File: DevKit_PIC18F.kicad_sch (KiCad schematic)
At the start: 25 parts, among them J1 PIC_ICSP_ICD, J2 USB_B, J4 RA_PORT, J5 RB_PORT, J6 RD_PORT, J7 RC_PORT, J8 RE_PORT, J9 2P_UART, SW1 SW_DIP, X1 16MHz

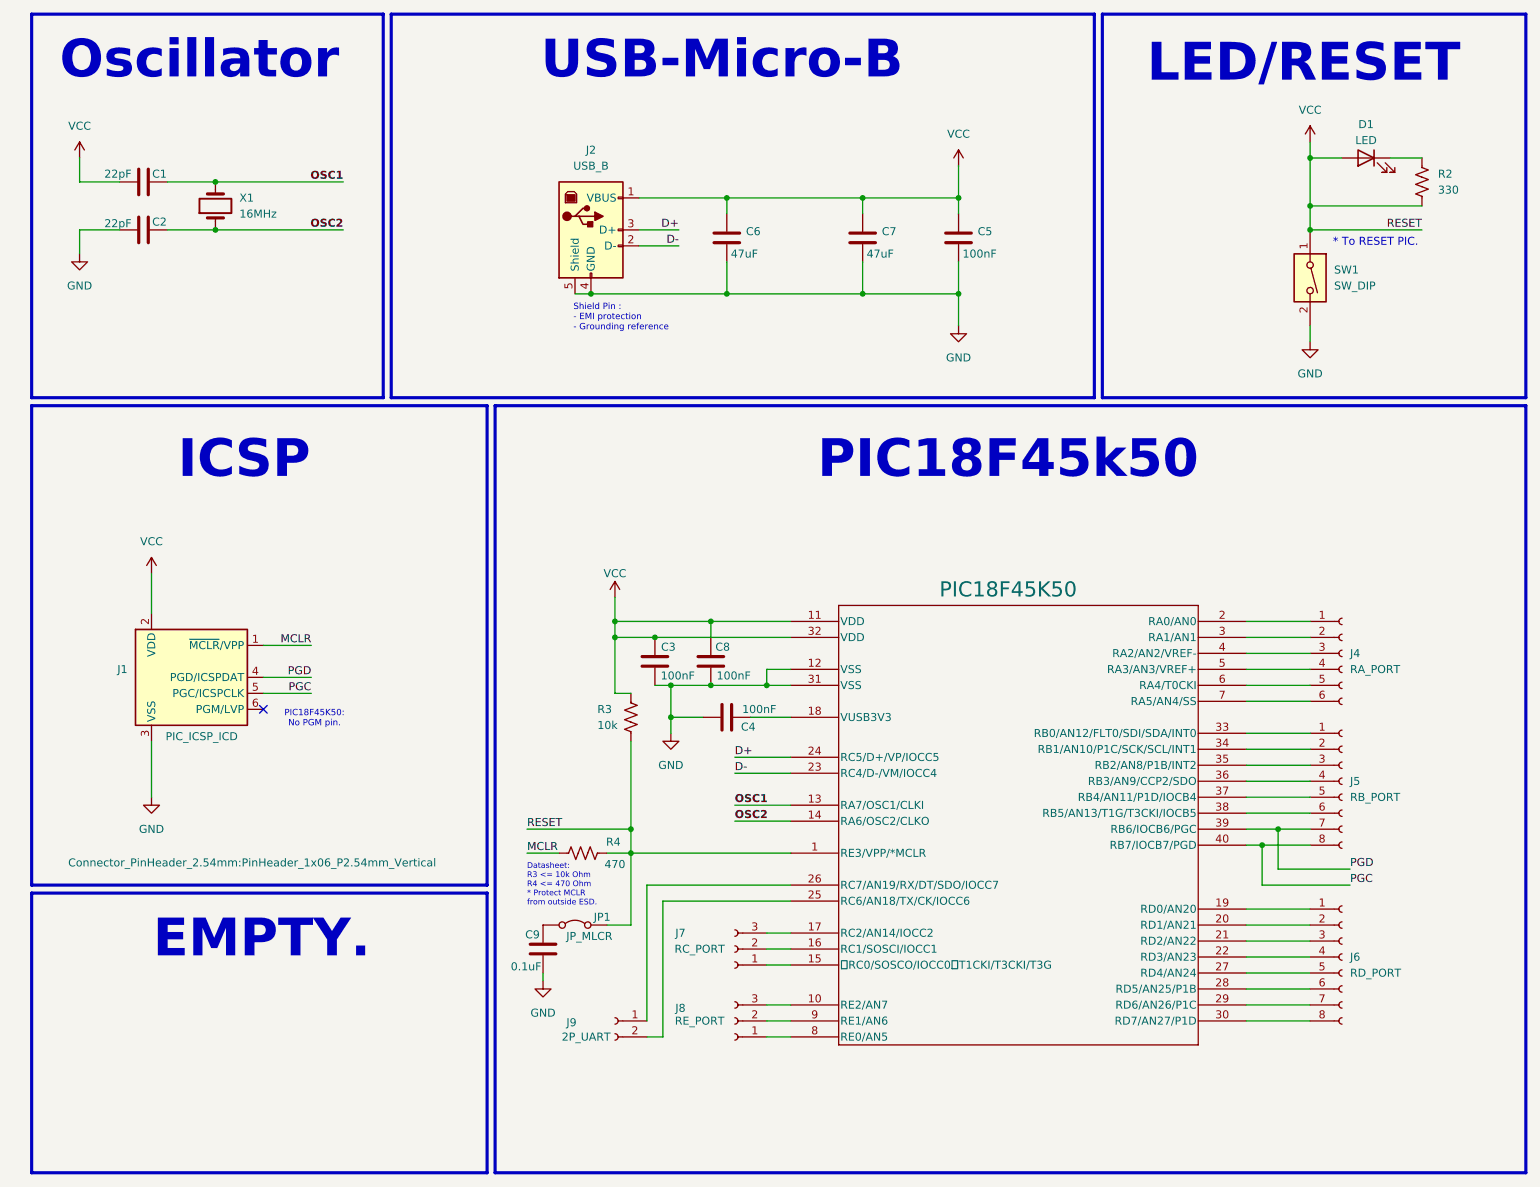
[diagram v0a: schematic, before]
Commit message: Change USB-B -> USB-C & Added EdgeCut.
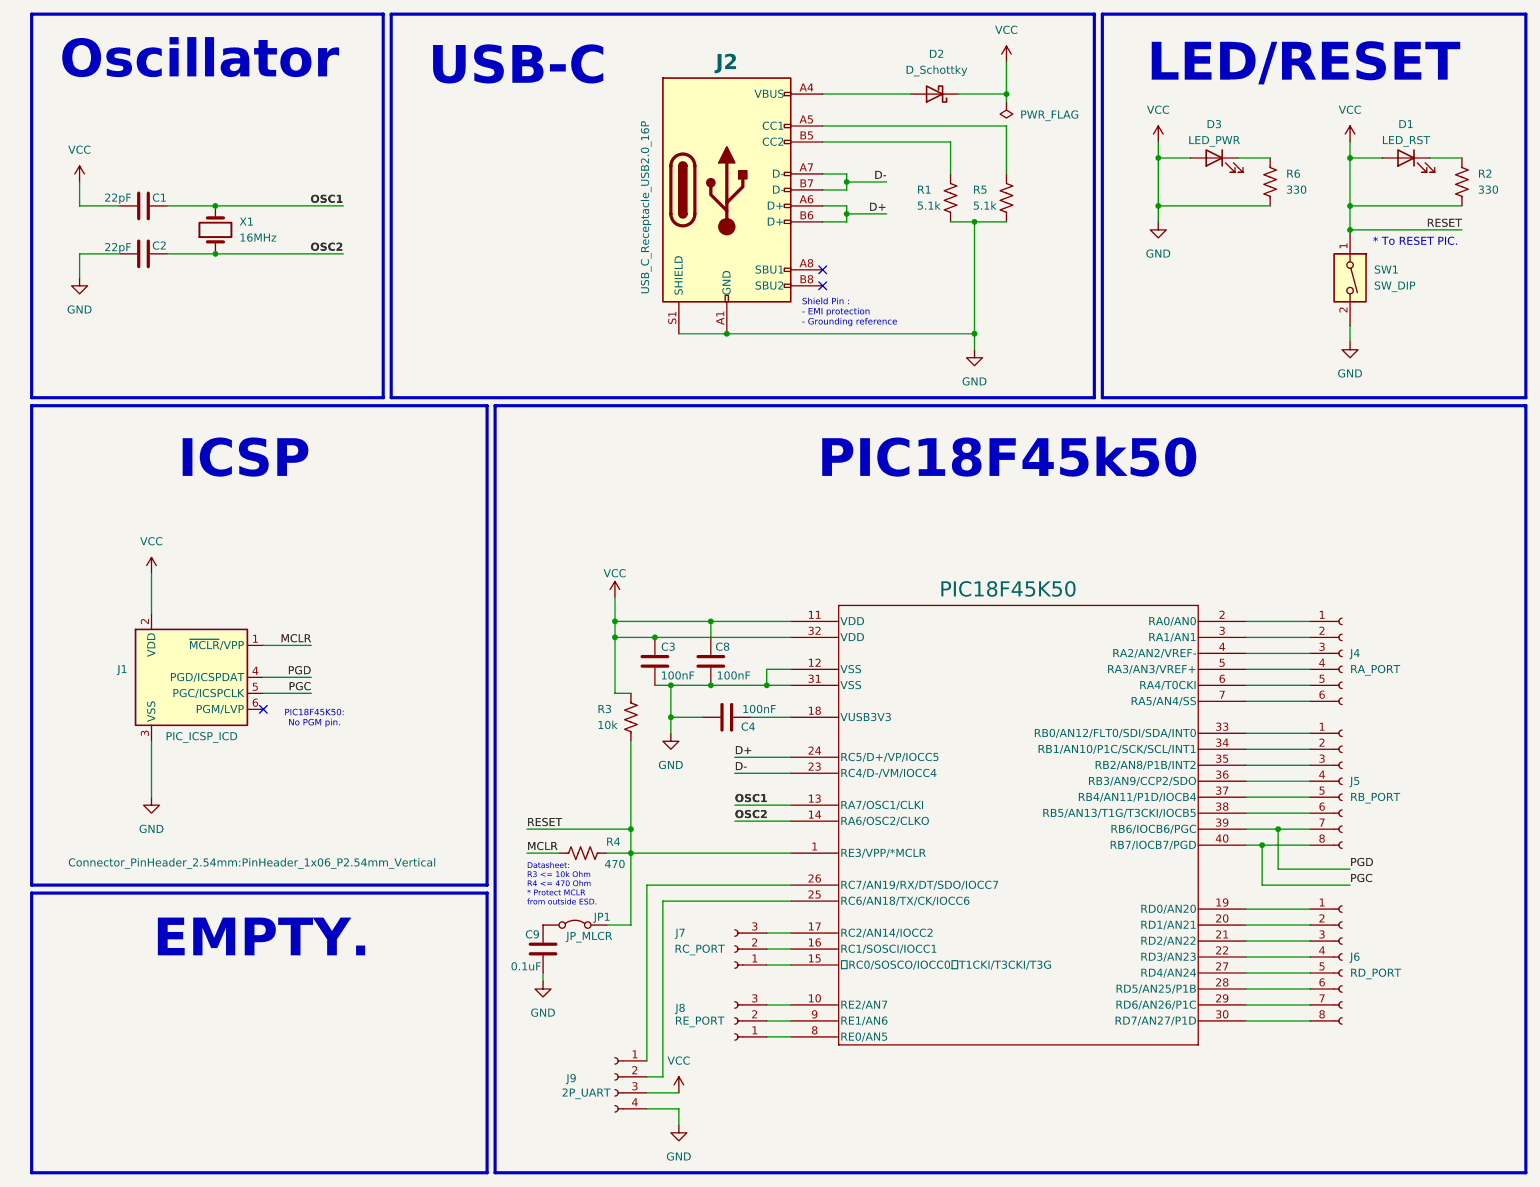
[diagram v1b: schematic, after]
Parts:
- removed C5: 100nF, Capacitor_THT:CP_Radial_D4.0mm_P2.00mm, symbol Device:C
- removed C6, C7: 47uF, Capacitor_THT:CP_Radial_D4.0mm_P2.00mm, symbol Device:C
- removed J2: USB_B, Connector_USB:USB_B_OST_USB-B1HSxx_Horizontal, symbol Connector:USB_B
- added D2: D_Schottky, Diode_THT:D_DO-34_SOD68_P7.62mm_Horizontal, symbol Device:D_Schottky
- added D3: LED_PWR, LED_THT:LED_D3.0mm_FlatTop, symbol Device:LED
- added J2: USB_C_Receptacle_USB2.0_16P, Connector_USB:USB_C_Receptacle_GCT_USB4085, symbol Connector:USB_C_Receptacle_USB2.0_16P
- added R1, R5: 5.1k, Resistor_THT:R_Axial_DIN0204_L3.6mm_D1.6mm_P5.08mm_Horizontal, symbol Device:R_US
- added R6: 330, Resistor_THT:R_Axial_DIN0204_L3.6mm_D1.6mm_P5.08mm_Horizontal, symbol Device:R_US
- D1: value LED -> LED_RST; footprint LED_THT:LED_D3.0mm -> LED_THT:LED_D3.0mm_FlatTop
- J9: footprint Connector_PinSocket_2.54mm:PinSocket_1x02_P2.54mm_Vertical -> Connector_PinSocket_2.54mm:PinSocket_1x04_P2.54mm_Vertical; symbol Connector:Conn_01x02_Socket -> Connector:Conn_01x04_Socket
- R3, R4: footprint Resistor_THT:R_Axial_DIN0207_L6.3mm_D2.5mm_P10.16mm_Horizontal -> Resistor_THT:R_Axial_DIN0204_L3.6mm_D1.6mm_P5.08mm_Horizontal
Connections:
- net VCC is gone; now on net GND: C1.2, C3.1, C8.1, D1.2 (A), J1.2 (VDD), JP1.2 (B), PIC18F45K50.1 (RE3/VPP/*MCLR), PIC18F45K50.11 (VDD), PIC18F45K50.32 (VDD), R2.2, R3.1, R3.2, R4.2, SW1.1
- net D+: now also J2.A6 (D+), J2.B6 (D+)
- net D-: now also J2.A7 (D-), J2.B7 (D-)
- net GND: now also J9.3 (Pin_3), J9.4 (Pin_4), D2.1 (K), D3.2 (A), J2.A1 (GND), J2.A12 (GND), J2.B1 (GND), J2.B12 (GND), J2.S1 (SHIELD), R1.2, R5.2, R6.2
- new net: D3.1 (K), R6.1
- new net: J2.A5 (CC1), R5.1
- new net: J2.B5 (CC2), R1.1
- new net: D2.2 (A), J2.A4 (VBUS), J2.A9 (VBUS), J2.B4 (VBUS), J2.B9 (VBUS)
- no-connect marks 1 -> 3
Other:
- note added: "USB-C"
- note removed: "USB-Micro-B"
- moved on the sheet: C1, C2, D1, R2, SW1, X1

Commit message: Routed & Finished Rev.1
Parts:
- J9: footprint Connector_PinSocket_2.54mm:PinSocket_1x04_P2.54mm_Vertical -> Connector_PinSocket_2.54mm:PinSocket_1x05_P2.54mm_Vertical; symbol Connector:Conn_01x04_Socket -> Connector:Conn_01x05_Socket
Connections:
- net GND: now also J9.5 (Pin_5); no longer J9.4 (Pin_4)
- net PGC: now also J5.7 (Pin_7), PIC18F45K50.39 (RB6/IOCB6/PGC); no longer J5.8 (Pin_8), PIC18F45K50.40 (RB7/IOCB7/PGD)
- net PGD: now also J5.8 (Pin_8), PIC18F45K50.40 (RB7/IOCB7/PGD); no longer J5.7 (Pin_7), PIC18F45K50.39 (RB6/IOCB6/PGC)
- no-connect marks 3 -> 4
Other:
- note added: "CTS"
- note added: "GND"
- note added: "RX"
- note added: "TX"
- note added: "USB-TTL-FT232"
- note added: "VCC"

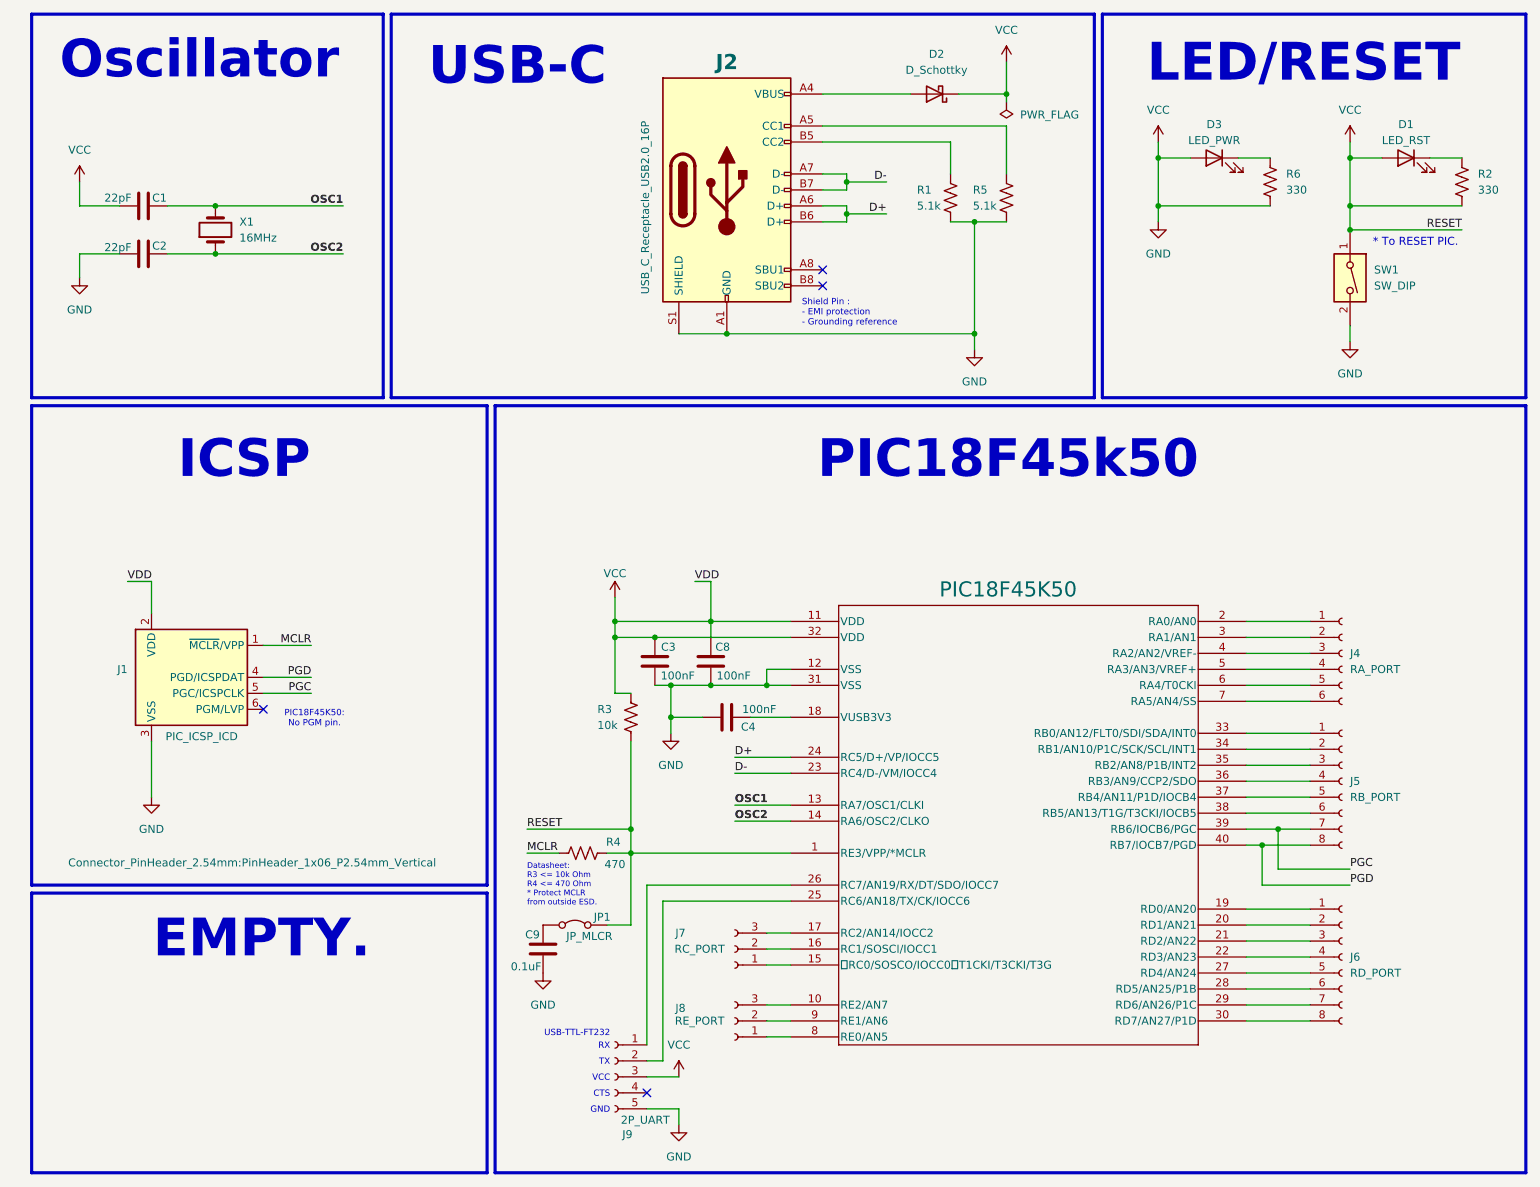
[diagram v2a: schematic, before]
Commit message: Fixed Crystal Error & re-routed some more.
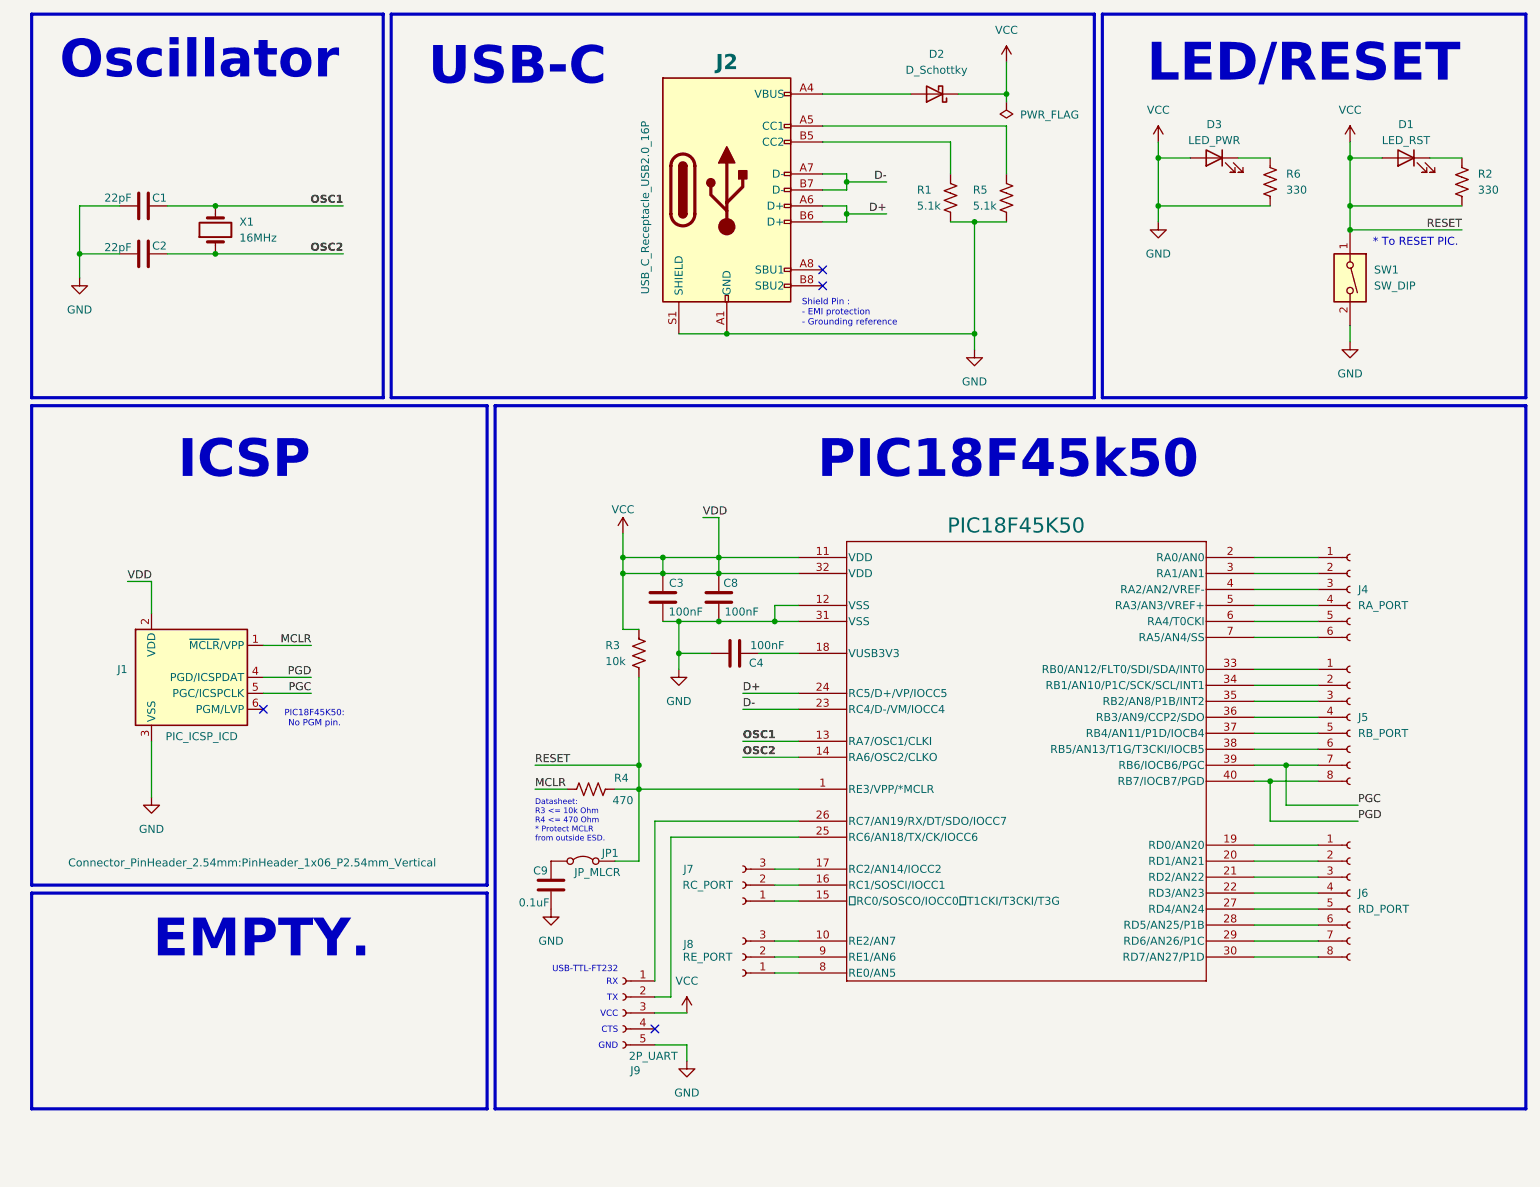
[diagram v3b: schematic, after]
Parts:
- C1, C2: footprint Capacitor_THT:CP_Radial_D4.0mm_P2.00mm -> Capacitor_THT:C_Disc_D3.0mm_W1.6mm_P2.50mm
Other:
- moved on the sheet: C3, C4, C8, C9, J4, J5, J6, J7, J8, J9, JP1, PIC18F45K50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

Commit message: refine routing
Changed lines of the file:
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@@
+	(wire
+		(pts
+			(xy 114.3 101.6) (xy 114.3 104.14)
+		)
+		(stroke
+			(width 0)
+			(type default)
+		)
+	)
 	(wire
 		(pts
